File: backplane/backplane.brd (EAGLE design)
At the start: 177 x 80 mm, 10 parts, among them J1 09232486825, J2 09232486825, J3 09232486825, J4 09232486825, J5 09232486825, J6 09232486825, J7 09232486825, J8 09232486825, J9 TB009-508-04BE

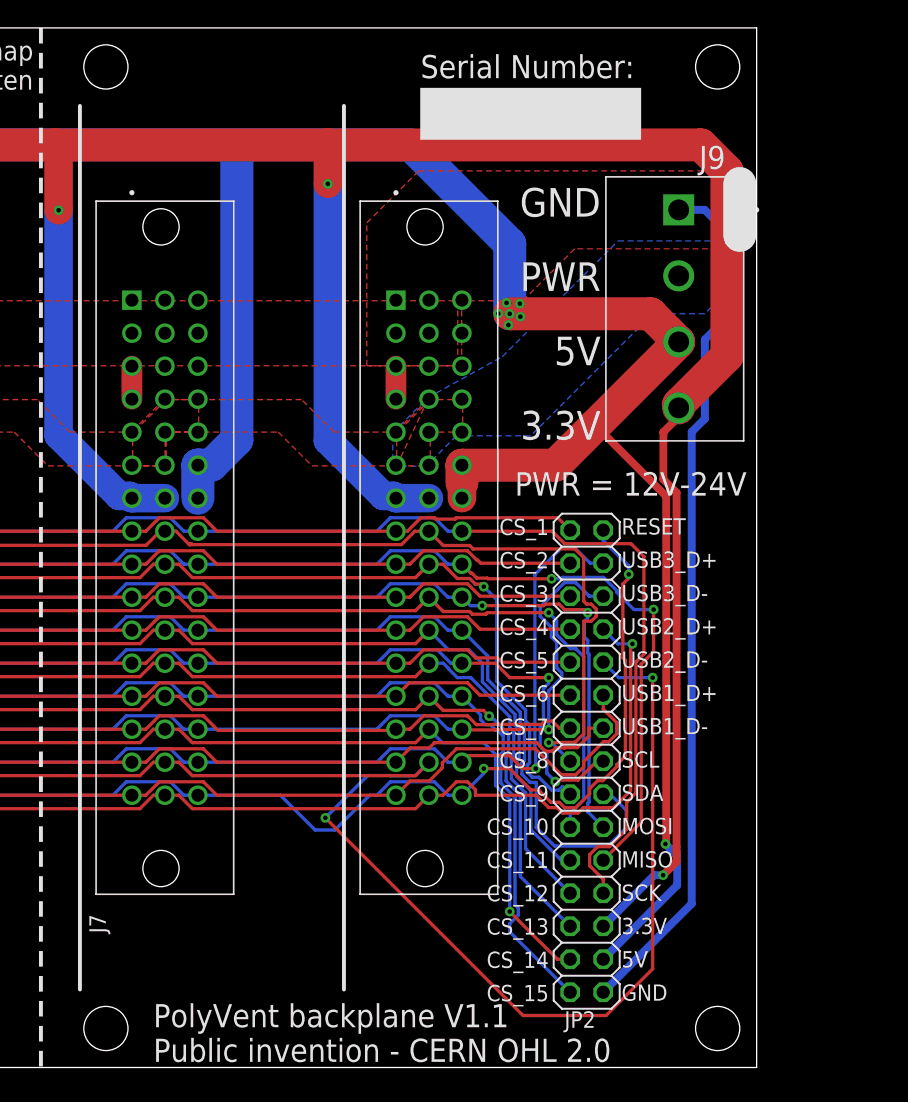
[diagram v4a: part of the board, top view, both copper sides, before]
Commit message: final mods to the boards, next commit will add the CAM data, it will be the final commit before the polyvent V2.1 design merge, and I'm ready to order boards
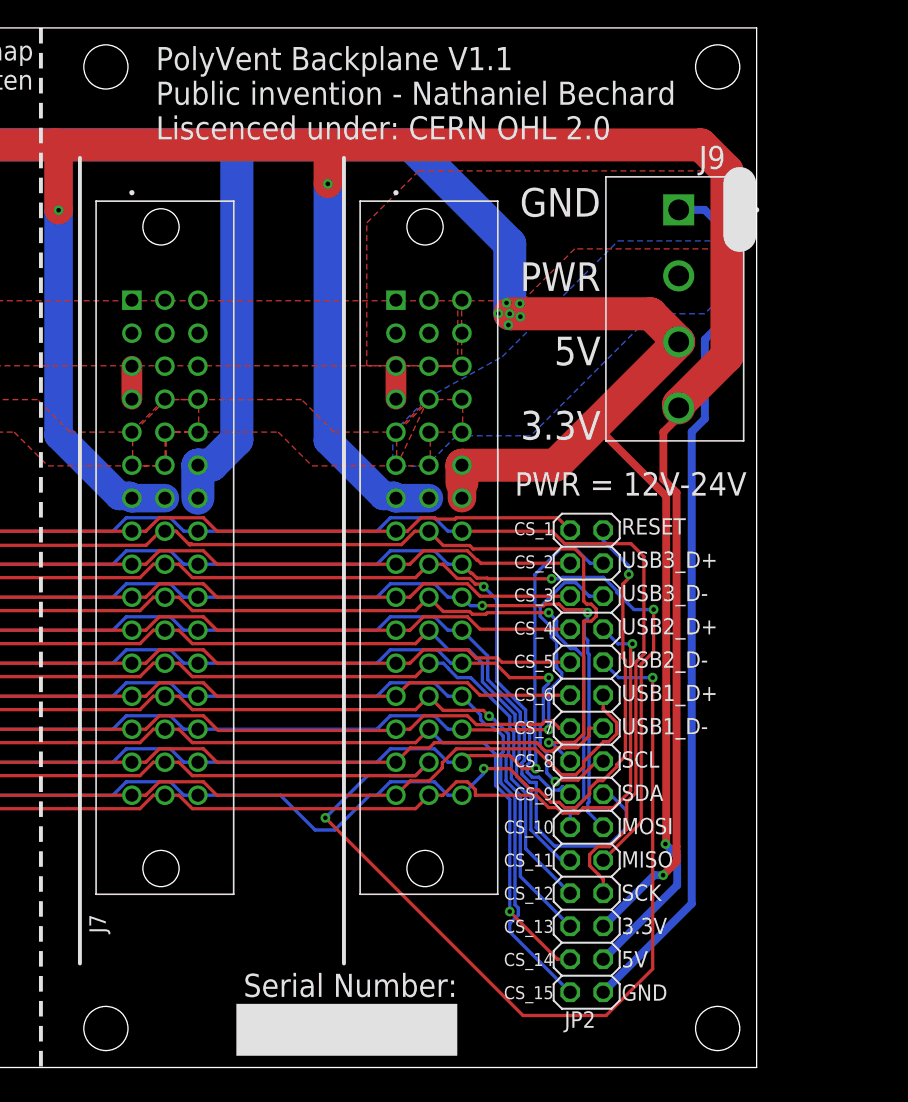
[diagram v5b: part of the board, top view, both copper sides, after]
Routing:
- net 5V: track 439.0 -> 443.6 mm
- net GND: track 87.4 -> 90.0 mm
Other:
- board text added: "PolyVent Backplane V1.1 Public invention - Nathaniel Bechard Liscenced under: CERN OHL 2.0"
- board text removed: "PolyVent backplane V1.1 Public invention - CERN OHL 2.0"
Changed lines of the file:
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@@
 <grid distance="1" unitdist="mm" unit="mm" style="lines" multiple="1" display="no" altdistance="0.01" altunitdist="mm" altunit="mm"/>
 <layers>
-<layer number="1" name="Top" color="4" fill="1" visible="no" active="yes"/>
+<layer number="1" name="Top" color="4" fill="1" visible="yes" active="yes"/>
 <layer number="2" name="Route2" color="16" fill="1" visible="no" active="no"/>
 <layer number="3" name="Route3" color="17" fill="1" visible="no" active="no"/>
@@
 <layer number="14" name="Route14" color="22" fill="1" visible="no" active="no"/>
 <layer number="15" name="Route15" color="23" fill="1" visible="no" active="no"/>
-<layer number="16" name="Bottom" color="1" fill="1" visible="no" active="yes"/>
+<layer number="16" name="Bottom" color="1" fill="1" visible="yes" active="yes"/>
 <layer number="17" name="Pads" color="2" fill="1" visible="yes" active="yes"/>
 <layer number="18" name="Vias" color="2" fill="1" visible="yes" active="yes"/>
@@
 <layer number="56" name="wert" color="7" fill="1" visible="no" active="yes"/>
 <layer number="57" name="tCAD" color="7" fill="1" visible="no" active="no"/>
+<layer number="58" name="tCAD" color="7" fill="1" visible="no" active="no"/>
 <layer number="59" name="tCarbon" color="7" fill="1" visible="no" active="no"/>
 <layer number="60" name="bCarbon" color="7" fill="1" visible="no" active="no"/>
@@
 <layer number="115" name="ReferenceISLANDS" color="7" fill="1" visible="yes" active="yes"/>
 <layer number="116" name="Patch_BOT" color="9" fill="4" visible="yes" active="yes"/>
+<layer number="117" name="BACKMAAT1" color="7" fill="1" visible="yes" active="yes"/>
 <layer number="118" name="Rect_Pads" color="7" fill="1" visible="yes" active="yes"/>
+<layer number="119" name="KAP_TEKEN" color="7" fill="1" visible="yes" active="yes"/>
+<layer number="120" name="KAP_MAAT1" color="7" fill="1" visible="yes" active="yes"/>
 <layer number="121" name="_tsilk" color="7" fill="1" visible="yes" active="yes"/>
 <layer number="122" name="_bsilk" color="7" fill="1" visible="yes" active="yes"/>
@@
 <layer number="128" name="_bValues" color="7" fill="1" visible="yes" active="yes"/>
 <layer number="129" name="Mask" color="7" fill="1" visible="yes" active="yes"/>
+<layer number="130" name="SMDSTROOK" color="7" fill="1" visible="yes" active="yes"/>
 <layer number="131" name="tAdjust" color="7" fill="1" visible="yes" active="yes"/>
 <layer number="132" name="bAdjust" color="7" fill="1" visible="yes" active="yes"/>
+<layer number="133" name="bottom_silk" color="7" fill="1" visible="yes" active="yes"/>
 <layer number="144" name="Drill_legend" color="7" fill="1" visible="yes" active="yes"/>
+<layer number="145" name="DrillLegend_01-16" color="2" fill="9" visible="no" active="yes"/>
 <layer number="150" name="Notes" color="7" fill="1" visible="yes" active="yes"/>
 <layer number="151" name="HeatSink" color="7" fill="1" visible="no" active="yes"/>
@@
 <wire x1="121.92" y1="80" x2="121.92" y2="0" width="0.3" layer="26" style="shortdash"/>
 <wire x1="175.7" y1="68.03" x2="175.7" y2="64.03" width="2.54" layer="25"/>
-<text x="130.57" y="0.43" size="1.778" layer="25">PolyVent backplane V1.1
-Public invention - CERN OHL 2.0</text>
-<rectangle x1="157.61" y1="64.89" x2="161.61" y2="81.89" layer="25" rot="R90"/>
-<text x="167.6" y="77.91" size="1.778" layer="25" rot="R180">Serial Number:</text>
+<rectangle x1="143.46" y1="-5.6" x2="147.46" y2="11.4" layer="25" rot="R90"/>
+<text x="153.97" y="7.21" size="1.778" layer="25" rot="R180">Serial Number:</text>
 <wire x1="3" y1="6" x2="3" y2="74" width="0.3" layer="25"/>
 <wire x1="23.32" y1="6" x2="23.32" y2="74" width="0.3" layer="25"/>
@@
 <wire x1="84.28" y1="6" x2="84.28" y2="74" width="0.3" layer="25"/>
 <wire x1="104.6" y1="6" x2="104.6" y2="74" width="0.3" layer="25"/>
-<wire x1="124.92" y1="6" x2="124.92" y2="74" width="0.3" layer="25"/>
-<wire x1="145.24" y1="6" x2="145.24" y2="74" width="0.3" layer="25"/>
-<text x="161.01" y="5.1" size="1.25" layer="25" distance="105" align="bottom-right">CS_1
+<wire x1="124.92" y1="8" x2="124.92" y2="70" width="0.3" layer="25"/>
+<wire x1="145.24" y1="8" x2="145.24" y2="70" width="0.3" layer="25"/>
+<text x="161.38" y="5.26" size="1" layer="25" distance="155" align="bottom-right">CS_1
 CS_2
 CS_3
@@
 GND</text>
 <text x="158.38" y="44.01" size="1.8" layer="25">PWR = 12V-24V</text>
+<text x="130.77" y="71.42" size="1.778" layer="25">PolyVent Backplane V1.1
+Public invention - Nathaniel Bechard
+Liscenced under: CERN OHL 2.0</text>
 </plain>
 <attributes>
@@
 <attribute name="PRICE" value="None" x="171" y="66" size="1.778" layer="27" rot="R270" display="off"/>
 <attribute name="PURCHASE-URL" value="https://pricing.snapeda.com/search/part/TB009-508-04BE/?ref=eda" x="171" y="66" size="1.778" layer="27" rot="R270" display="off"/>
-<attribute name="VALUE" x="172.15" y="70.54" size="1.778" layer="27" rot="R180"/>
+<attribute name="VALUE" x="166.4" y="67.81" size="1.778" layer="27" rot="R270"/>
 </element>
 <element name="JP2" library="pinhead" library_urn="urn:adsk.eagle:library:325" package="2X15" package3d_urn="urn:adsk.eagle:package:22427/2" value="" x="163.92" y="23.57" smashed="yes" rot="R90">
@@
 <wire x1="172" y1="12.6" x2="172" y2="48.91346875" width="0.6096" layer="16"/>
 <wire x1="175" y1="64" x2="173" y2="66" width="0.6096" layer="16"/>
-<wire x1="151.78" y1="53.97" x2="154.32" y2="53.97" width="0" layer="19" extent="1-1"/>
+<wire x1="154.32" y1="53.97" x2="151.78" y2="53.97" width="0.1524" layer="1"/>
 </signal>
 <signal name="24V/12V" class="1">
@@
 <wire x1="170.8824" y1="16.2990375" x2="170.8824" y2="14.0224" width="0.6096" layer="16"/>
 <wire x1="170.8824" y1="14.0224" x2="165.19" y2="8.33" width="0.6096" layer="16"/>
-<wire x1="158.82" y1="57.78" x2="158.78" y2="58.78" width="0" layer="19" extent="1-1"/>
-<wire x1="158" y1="58" x2="158.82" y2="57.78" width="0" layer="19" extent="1-1"/>
-<wire x1="157.89" y1="57.14" x2="158" y2="58" width="0" layer="19" extent="1-1"/>
-<wire x1="157.75" y1="58.84" x2="158" y2="58" width="0" layer="19" extent="1-1"/>
-<wire x1="157.12" y1="58.02" x2="158" y2="58" width="0" layer="19" extent="1-1"/>
+<wire x1="158" y1="58" x2="157.89" y2="57.89" width="0.1524" layer="1"/>
+<wire x1="157.89" y1="57.89" x2="157.89" y2="57.14" width="0.1524" layer="1"/>
+<wire x1="157.75" y1="58.84" x2="158" y2="58.59" width="0.1524" layer="1"/>
+<wire x1="158" y1="58.59" x2="158" y2="58" width="0.1524" layer="1"/>
+<wire x1="158" y1="58" x2="157.14" y2="58" width="0.1524" layer="1"/>
+<wire x1="157.14" y1="58" x2="157.12" y2="58.02" width="0.1524" layer="1"/>
+<wire x1="158" y1="58" x2="158.6" y2="58" width="0.1524" layer="1"/>
+<wire x1="158.6" y1="58" x2="158.82" y2="57.78" width="0.1524" layer="1"/>
+<wire x1="158.82" y1="57.78" x2="158.78" y2="57.82" width="0.1524" layer="1"/>
+<wire x1="158.78" y1="57.82" x2="158.78" y2="58.78" width="0.1524" layer="1"/>
 </signal>
 <signal name="SCK">
